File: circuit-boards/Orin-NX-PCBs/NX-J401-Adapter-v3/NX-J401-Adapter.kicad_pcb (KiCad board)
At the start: 4 copper layers, 109.9 x 79 mm, 52 parts, among them J1 18V_OUT, J10 HDMI, J11 HDMI, J2 MIPI, J3 CAN-NX, J4 MIPI, J5 NX-BUTTON, J6 CAN-NX, J7 CAN-NX, J8 CONSOLE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

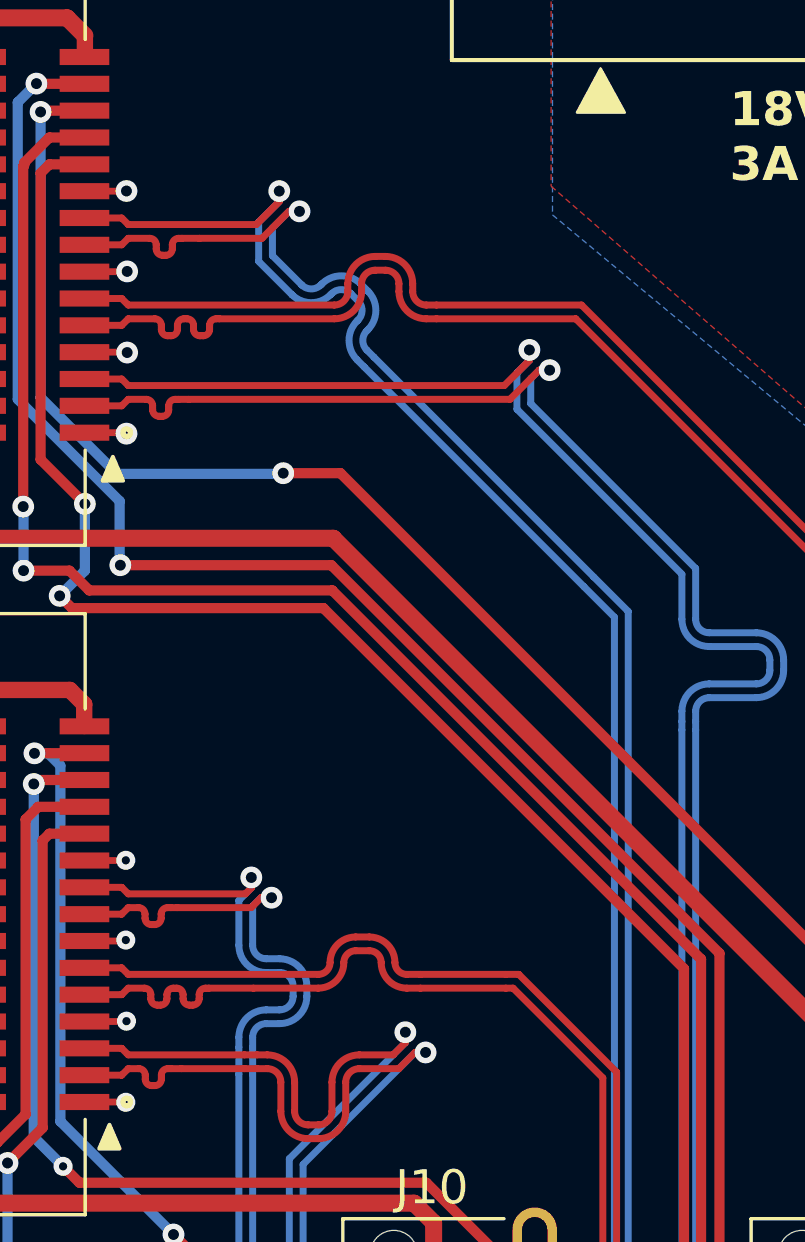
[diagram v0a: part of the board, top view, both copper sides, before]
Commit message: Add ground vias near diff pair vias to improve signal integrity.
Signed-off-by: Scott <sgberman1@gmail.com>
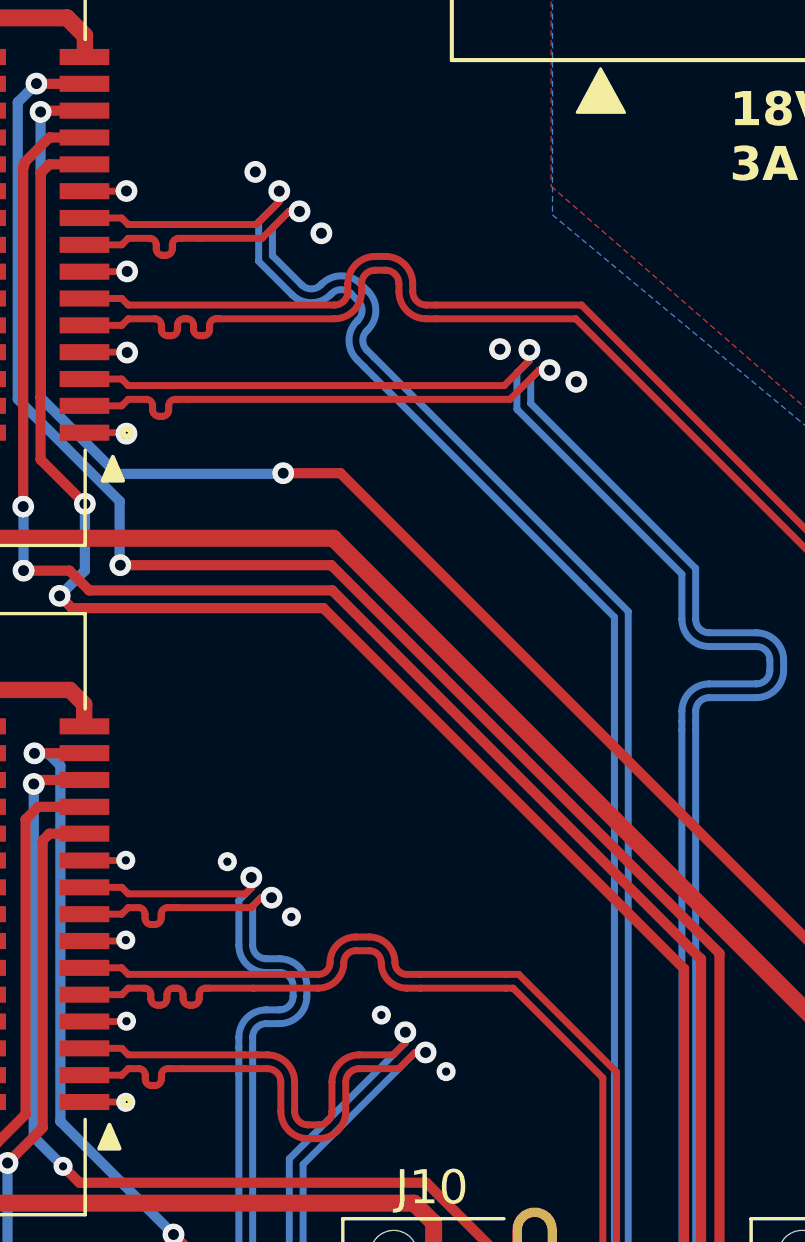
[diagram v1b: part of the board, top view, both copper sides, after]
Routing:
- net /MIPI-HDMI-2/GND_MIPI: vias 4 -> 8
- net /MIPI-HDMI-1/GND_MIPI: vias 4 -> 8
